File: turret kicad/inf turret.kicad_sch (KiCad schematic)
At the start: 6 parts, among them J1 Conn_01x06_Pin, J3 Conn_01x03_Pin, U1 XIAO-ESP32S3

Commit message: update the pcb a bit
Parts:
- added C1: 0.1µF, Capacitor_SMD:C_0805_2012Metric, symbol Device:C
- C2: footprint Capacitor_SMD:C_0805_2012Metric -> Capacitor_SMD:C_1206_3216Metric
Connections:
- net +5V: now also C1.2
- net GND: now also C1.1
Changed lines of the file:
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@@
+		(color 0 0 0 0)
+	)
+	(junction
+		(at 246.38 38.1)
+		(diameter 0)
 		(color 0 0 0 0)
 	)
@@
 	(wire
 		(pts
-			(xy 245.11 35.56) (xy 245.11 38.1)
+			(xy 259.08 35.56) (xy 259.08 38.1)
 		)
 		(stroke
@@
 	(wire
 		(pts
-			(xy 238.76 38.1) (xy 245.11 38.1)
+			(xy 238.76 38.1) (xy 246.38 38.1)
 		)
 		(stroke
@@
 		(pts
 			(xy 191.77 33.02) (xy 194.31 33.02)
+		)
+		(stroke
+			(width 0)
+			(type default)
+		)
+	)
+	(wire
+		(pts
+			(xy 246.38 38.1) (xy 259.08 38.1)
 		)
 		(stroke
@@
 	)
 	(symbol
+		(lib_id "power:GND")
+		(at 246.38 30.48 0)
+		(mirror x)
+		(unit 1)
+		(exclude_from_sim no)
+		(in_bom yes)
+		(on_board yes)
+		(dnp no)
+		(property "Reference" "#PWR09"
+			(at 246.38 24.13 0)
+			(effects
+				(font
+					(size 1.27 1.27)
+				)
+				(hide yes)
+			)
+		)
+		(property "Value" "GND"
+			(at 246.38 25.4 0)
+			(effects
+				(font
+					(size 1.27 1.27)
+				)
+			)
+		)
+		(property "Footprint" ""
+			(at 246.38 30.48 0)
+			(effects
+				(font
+					(size 1.27 1.27)
+				)
+				(hide yes)
+			)
+		)
+		(property "Datasheet" ""
+			(at 246.38 30.48 0)
+			(effects
+				(font
+					(size 1.27 1.27)
+				)
+				(hide yes)
+			)
+		)
+		(property "Description" "Power symbol creates a global label with name \"GND\" , ground"
+			(at 246.38 30.48 0)
+			(effects
+				(font
+					(size 1.27 1.27)
+				)
+				(hide yes)
+			)
+		)
+		(pin "1"
+		)
+		(instances
+			(project "inf turret"
+				(path "/c2234474-1ef0-49db-bc4a-00d54e6bbb25"
+					(reference "#PWR09")
+					(unit 1)
+				)
+			)
+		)
+	)
+	(symbol
 		(lib_id "Connector:Conn_01x03_Pin")
 		(at 109.22 74.93 0)
@@
 	)
 	(symbol
+		(lib_id "Device:C")
+		(at 246.38 34.29 0)
+		(unit 1)
+		(exclude_from_sim no)
+		(in_bom yes)
+		(on_board yes)
+		(dnp no)
+		(fields_autoplaced yes)
+		(property "Reference" "C1"
+			(at 250.19 33.0199 0)
+			(effects
+				(font
+					(size 1.27 1.27)
+				)
+				(justify left)
+			)
+		)
+		(property "Value" "0.1µF"
+			(at 250.19 35.5599 0)
+			(effects
+				(font
+					(size 1.27 1.27)
+				)
+				(justify left)
+			)
+		)
+		(property "Footprint" "Capacitor_SMD:C_0805_2012Metric"
+			(at 247.3452 38.1 0)
+			(effects
+				(font
+					(size 1.27 1.27)
+				)
+				(hide yes)
+			)
+		)
+		(property "Datasheet" "~"
+			(at 246.38 34.29 0)
+			(effects
+				(font
+					(size 1.27 1.27)
+				)
+				(hide yes)
+			)
+		)
+		(property "Description" "Unpolarized capacitor"
+			(at 246.38 34.29 0)
+			(effects
+				(font
+					(size 1.27 1.27)
+				)
+				(hide yes)
+			)
+		)
+		(pin "1"
+		)
+		(pin "2"
+		)
+		(instances
+			(project ""
+				(path "/c2234474-1ef0-49db-bc4a-00d54e6bbb25"
+					(reference "C1")
+					(unit 1)
+				)
+			)
+		)
+	)
+	(symbol
 		(lib_id "power:GND")
 		(at 238.76 30.48 0)
@@
 			)
 		)
-		(property "Footprint" "Capacitor_SMD:C_0805_2012Metric"
+		(property "Footprint" "Capacitor_SMD:C_1206_3216Metric"
 			(at 239.7252 38.1 0)
 			(effects
@@
 	(symbol
 		(lib_id "power:+5V")
-		(at 245.11 35.56 0)
+		(at 259.08 35.56 0)
 		(unit 1)
 		(exclude_from_sim no)
@@
 		(fields_autoplaced yes)
 		(property "Reference" "#PWR03"
-			(at 245.11 39.37 0)
+			(at 259.08 39.37 0)
 			(effects
 				(font
@@
 		)
 		(property "Value" "+5V"
-			(at 245.11 30.48 0)
+			(at 259.08 30.48 0)
 			(effects
 				(font
@@
 		)
 		(property "Footprint" ""
-			(at 245.11 35.56 0)
+			(at 259.08 35.56 0)
 			(effects
 				(font
@@
 		)
 		(property "Datasheet" ""
-			(at 245.11 35.56 0)
+			(at 259.08 35.56 0)
 			(effects
 				(font
@@
 		)
 		(property "Description" "Power symbol creates a global label with name \"+5V\""
-			(at 245.11 35.56 0)
-			(effects
-				(font
+			(at 259.08 35.56 0)
+			(effects
+				(font

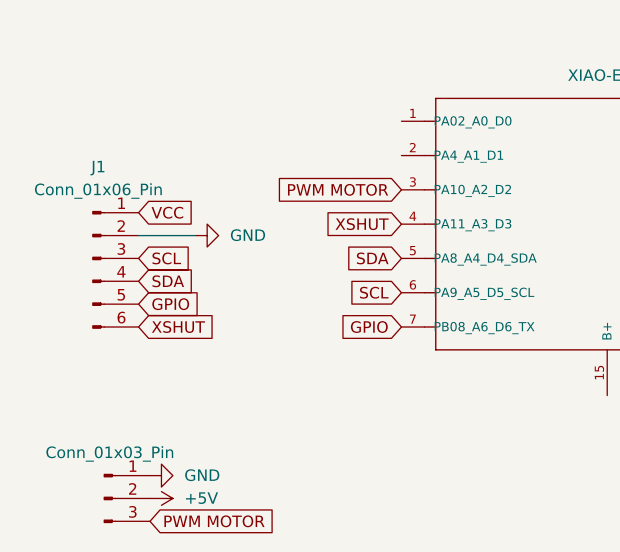
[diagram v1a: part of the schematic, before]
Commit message: add forth pin because i forgot the servo one
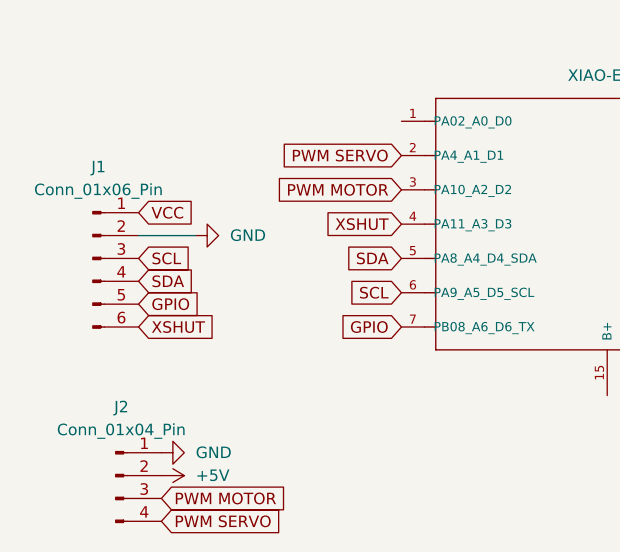
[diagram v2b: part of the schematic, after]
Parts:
- removed J3: Conn_01x03_Pin, Connector_PinHeader_2.54mm:PinHeader_1x03_P2.54mm_Vertical, symbol Connector:Conn_01x03_Pin
- added J2: Conn_01x04_Pin, Connector_PinHeader_2.54mm:PinHeader_1x04_P2.54mm_Vertical, symbol Connector:Conn_01x04_Pin
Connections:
- net +5V: now also J2.2 (Pin_2)
- net GND: now also J2.1 (Pin_1)
- net PWM MOTOR: now also J2.3 (Pin_3)
- net PWM SERVO: now reaches U1.2 (PA4_A1_D1)
- net PWM SERVO: now also J2.4 (Pin_4)
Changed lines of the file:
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@@
 		)
 	)
-	(global_label "PWM MOTOR"
+	(global_label "PWM SERVO"
 		(shape input)
-		(at 114.3 77.47 0)
+		(at 115.57 77.47 0)
 		(fields_autoplaced yes)
 		(effects
@@
 		)
 		(property "Intersheetrefs" "${INTERSHEET_REFS}"
-			(at 128.7756 77.47 0)
-			(effects
-				(font
-					(size 1.27 1.27)
-				)
-				(justify left)
+			(at 129.7432 77.47 0)
+			(effects
+				(font
+					(size 1.27 1.27)
+				)
+				(justify left)
+				(hide yes)
+			)
+		)
+	)
+	(global_label "PWM MOTOR"
+		(shape input)
+		(at 115.57 74.93 0)
+		(fields_autoplaced yes)
+		(effects
+			(font
+				(size 1.27 1.27)
+			)
+			(justify left)
+		)
+		(property "Intersheetrefs" "${INTERSHEET_REFS}"
+			(at 130.0456 74.93 0)
+			(effects
+				(font
+					(size 1.27 1.27)
+				)
+				(justify left)
+				(hide yes)
+			)
+		)
+	)
+	(global_label "PWM SERVO"
+		(shape input)
+		(at 142.24 36.83 180)
+		(fields_autoplaced yes)
+		(effects
+			(font
+				(size 1.27 1.27)
+			)
+			(justify right)
+		)
+		(property "Intersheetrefs" "${INTERSHEET_REFS}"
+			(at 128.0668 36.83 0)
+			(effects
+				(font
+					(size 1.27 1.27)
+				)
+				(justify right)
 				(hide yes)
 			)
@@
 	)
 	(symbol
+		(lib_id "Connector:Conn_01x04_Pin")
+		(at 110.49 72.39 0)
+		(unit 1)
+		(exclude_from_sim no)
+		(in_bom yes)
+		(on_board yes)
+		(dnp no)
+		(fields_autoplaced yes)
+		(property "Reference" "J2"
+			(at 111.125 64.77 0)
+			(effects
+				(font
+					(size 1.27 1.27)
+				)
+			)
+		)
+		(property "Value" "Conn_01x04_Pin"
+			(at 111.125 67.31 0)
+			(effects
+				(font
+					(size 1.27 1.27)
+				)
+			)
+		)
+		(property "Footprint" "Connector_PinHeader_2.54mm:PinHeader_1x04_P2.54mm_Vertical"
+			(at 110.49 72.39 0)
+			(effects
+				(font
+					(size 1.27 1.27)
+				)
+				(hide yes)
+			)
+		)
+		(property "Datasheet" "~"
+			(at 110.49 72.39 0)
+			(effects
+				(font
+					(size 1.27 1.27)
+				)
+				(hide yes)
+			)
+		)
+		(property "Description" "Generic connector, single row, 01x04, script generated"
+			(at 110.49 72.39 0)
+			(effects
+				(font
+					(size 1.27 1.27)
+				)
+				(hide yes)
+			)
+		)
+		(pin "4"
+		)
+		(pin "2"
+		)
+		(pin "1"
+		)
+		(pin "3"
+		)
+		(instances
+			(project ""
+				(path "/c2234474-1ef0-49db-bc4a-00d54e6bbb25"
+					(reference "J2")
+					(unit 1)
+				)
+			)
+		)
+	)
+	(symbol
 		(lib_id "power:GND")
 		(at 246.38 30.48 0)
@@
 	)
 	(symbol
-		(lib_id "Connector:Conn_01x03_Pin")
-		(at 109.22 74.93 0)
-		(unit 1)
-		(exclude_from_sim no)
-		(in_bom yes)
-		(on_board yes)
-		(dnp no)
-		(fields_autoplaced yes)
-		(property "Reference" "J3"
-			(at 109.855 67.31 0)
-			(effects
-				(font
-					(size 1.27 1.27)
-				)
-				(hide yes)
-			)
-		)
-		(property "Value" "Conn_01x03_Pin"
-			(at 109.855 69.85 0)
-			(effects
-				(font
-					(size 1.27 1.27)
-				)
-			)
-		)
-		(property "Footprint" "Connector_PinHeader_2.54mm:PinHeader_1x03_P2.54mm_Vertical"
-			(at 109.22 74.93 0)
-			(effects
-				(font
-					(size 1.27 1.27)
-				)
-				(hide yes)
-			)
-		)
-		(property "Datasheet" "~"
-			(at 109.22 74.93 0)
-			(effects
-				(font
-					(size 1.27 1.27)
-				)
-				(hide yes)
-			)
-		)
-		(property "Description" "Generic connector, single row, 01x03, script generated"
-			(at 109.22 74.93 0)
-			(effects
-				(font
-					(size 1.27 1.27)
-				)
-				(hide yes)
-			)
-		)
-		(pin "3"
-		)
-		(pin "1"
-		)
-		(pin "2"
-		)
-		(instances
-			(project ""
-				(path "/c2234474-1ef0-49db-bc4a-00d54e6bbb25"
-					(reference "J3")
-					(unit 1)
-				)
-			)
-		)
-	)
-	(symbol
 		(lib_id "Device:C")
 		(at 246.38 34.29 0)
@@
 	(symbol
 		(lib_id "power:+5V")
-		(at 114.3 74.93 270)
-		(unit 1)
-		(exclude_from_sim no)
-		(in_bom yes)
-		(on_board yes)
-		(dnp no)
-		(fields_autoplaced yes)
+		(at 115.57 72.39 270)
+		(unit 1)
+		(exclude_from_sim no)
+		(in_bom yes)
+		(on_board yes)
+		(dnp no)
 		(property "Reference" "#PWR07"
-			(at 110.49 74.93 0)
+			(at 111.76 72.39 0)
 			(effects
 				(font
@@
 		)
 		(property "Value" "+5V"
-			(at 118.11 74.9299 90)
+			(at 119.38 72.3899 90)
 			(effects
 				(font
@@
 		)
 		(property "Footprint" ""
-			(at 114.3 74.93 0)
+			(at 115.57 72.39 0)
 			(effects
 				(font
@@
 		)
 		(property "Datasheet" ""
-			(at 114.3 74.93 0)
+			(at 115.57 72.39 0)
 			(effects
 				(font
@@
 		)
 		(property "Description" "Power symbol creates a global label with name \"+5V\""
-			(at 114.3 74.93 0)
+			(at 115.57 72.39 0)
 			(effects
 				(font
@@
 	(symbol
 		(lib_id "power:GND")
-		(at 114.3 72.39 90)
-		(unit 1)
-		(exclude_from_sim no)
-		(in_bom yes)
-		(on_board yes)
-		(dnp no)
-		(fields_autoplaced yes)
+		(at 115.57 69.85 90)
+		(unit 1)
+		(exclude_from_sim no)
+		(in_bom yes)
+		(on_board yes)
+		(dnp no)
 		(property "Reference" "#PWR04"
-			(at 120.65 72.39 0)
+			(at 121.92 69.85 0)
 			(effects
 				(font
@@
 		)
 		(property "Value" "GND"
-			(at 118.11 72.3899 90)
+			(at 119.38 69.8499 90)
 			(effects
 				(font
@@
 		)
 		(property "Footprint" ""
-			(at 114.3 72.39 0)
+			(at 115.57 69.85 0)
 			(effects
 				(font
@@
 		)
 		(property "Datasheet" ""
-			(at 114.3 72.39 0)
+			(at 115.57 69.85 0)
 			(effects
 				(font
@@
 		)
 		(property "Description" "Power symbol creates a global label with name \"GND\" , ground"
-			(at 114.3 72.39 0)
-			(effects
-				(font
+			(at 115.57 69.85 0)
+			(effects
+				(font
